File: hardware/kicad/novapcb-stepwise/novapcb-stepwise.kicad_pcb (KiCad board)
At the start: 6 copper layers, 105 x 85 mm, 129 parts, among them J1 USB-C_2.0, J10 CRSF_solder_pad, J11 ESC_solder_pad, J12 ESC_solder_pad, J13 ESC_solder_pad, J14 ESC_solder_pad, J15 ESC_solder_pad, J16 ESC_solder_pad, J17 ESC_solder_pad, J18 ESC_solder_pad, J19 MAUCH2_6P, J2 microSD_DM3AT, J20 CAN_4P, J3 TELEM_6P, J4 MAUCH_6P, J5 GPS_MAG_10P, J9 SWD_10P, Q2 AO3401A, Q3 AO4262E, Q4 AO4262E, Q5 AO3400A, U1 STM32H743VITx, U11 LM74700-Q1, U12 LM74700-Q1, U13 LP5907MFX-3.3, U14 TJA1051TK/3, U15 PESD2CAN, U2 AP2112K-3.3, U3 ICM-42688-P_LGA-14_2.5x3mm_P0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, U4 DPS310, U5 USBLC6-2P6, U6 TPS25940A, U7 LPS22HB, U8 BMI088, U9 LSM6DSV16X, Y1 8MHz

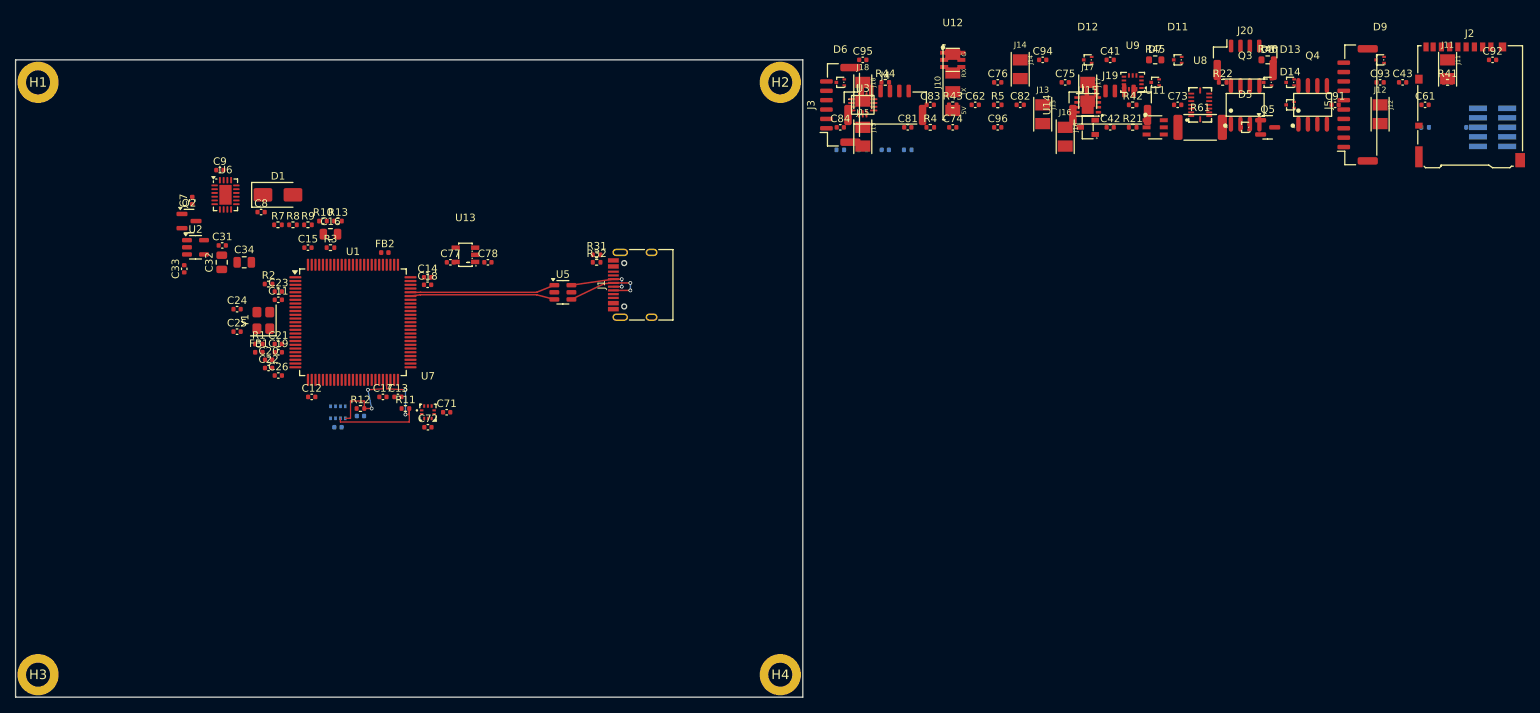
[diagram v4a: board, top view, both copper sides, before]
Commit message: hw: C↔B integration — +3V3 plane on In4.Cu + B-internal traces
Routes power rails B → C per master 2026-05-23 plan. DRC=0, gate12 v3
PASS at MCU 73.98°C (+6.02°C margin to 80°C, +1.02°C to lock target).

Strategy after F.Cu-zone + F.Cu-trace attempts surfaced MCU-pin-row +
GND-pad shorts: use inner-layer power plane.

  - +3V3 main rail: filled zone on In4.Cu, X=15..95, Y=18..52.
  - 18 vias at WIDE +3V3 pads (caps + sensor pads) connect F.Cu pad
    to In4.Cu plane.
  - 3 MCU VDD pins (U1.11, U1.75, U1.100) connected via 0.2mm F.Cu
    stubs to extra vias placed in clear space (avoiding Y1 GND, pin
    rows, and I2C2_SDA traces).
  - 2 MCU VDD pins (U1.27, U1.50) DEFERRED — south-stub crosses
    existing I2C2_SDA route; need B.Cu workaround in C↔E-2 step.
  - R11 +3V3 pull-up via DEFERRED — only marginal clearance (0.0035mm
    under rule) to existing I2C2_SDA via.

  - +3V3_IMU_PRE chain B-internal: FB2.2 → C77.1 → U13.1 + U13.3 stub.
    Routes use W=0.20mm and turn at (60.0, 24.0) to clear C77.2 GND
    and U13.4 NC pads (1.10mm wide SOT-23 pads — wider than expected).

  - +5V_BEC DEFERRED — discovered U2.1 input net is +5V (not +5V_BEC).
    The +5V source comes from A-zone Q3/Q4 OR-FETs which are unplaced.
    A↔B routing handles this in next phase.

Two placement fixes also in this commit:
  - update_outline_v11.py: hole inset 3.0 → 3.25mm so 5.5mm pads have
    0.5mm edge clearance (1.25mm fix preserves c-to-c ~98.5×78.5mm,
    within mechanical tolerance of master's "3mm inset" directive).
  - step5_place_B.py: C77 moved (58,27)→(56.5,27) so its GND pad
    clears U13.5 (+3V3_IMU) — pre-existing baseline DRC issue from
    the 105×85 outline transition.

gate12 v3 thermal check (full v1.1 load):
  Energy balance Q_in=1.7165 W, Q_out=1.7218 W, +0.31% PASS
  T_avg=69.29°C, T_max=78.14°C
  Tj_U1 (MCU) = 73.98°C  margin to 80°C = +6.02°C  LOCK
  Tj_U2 (LDO) = 70.01°C  margin to 80°C = +10.00°C LOCK
  All placed parts LOCK; planned positions (Q3, Q4, U14) TIGH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
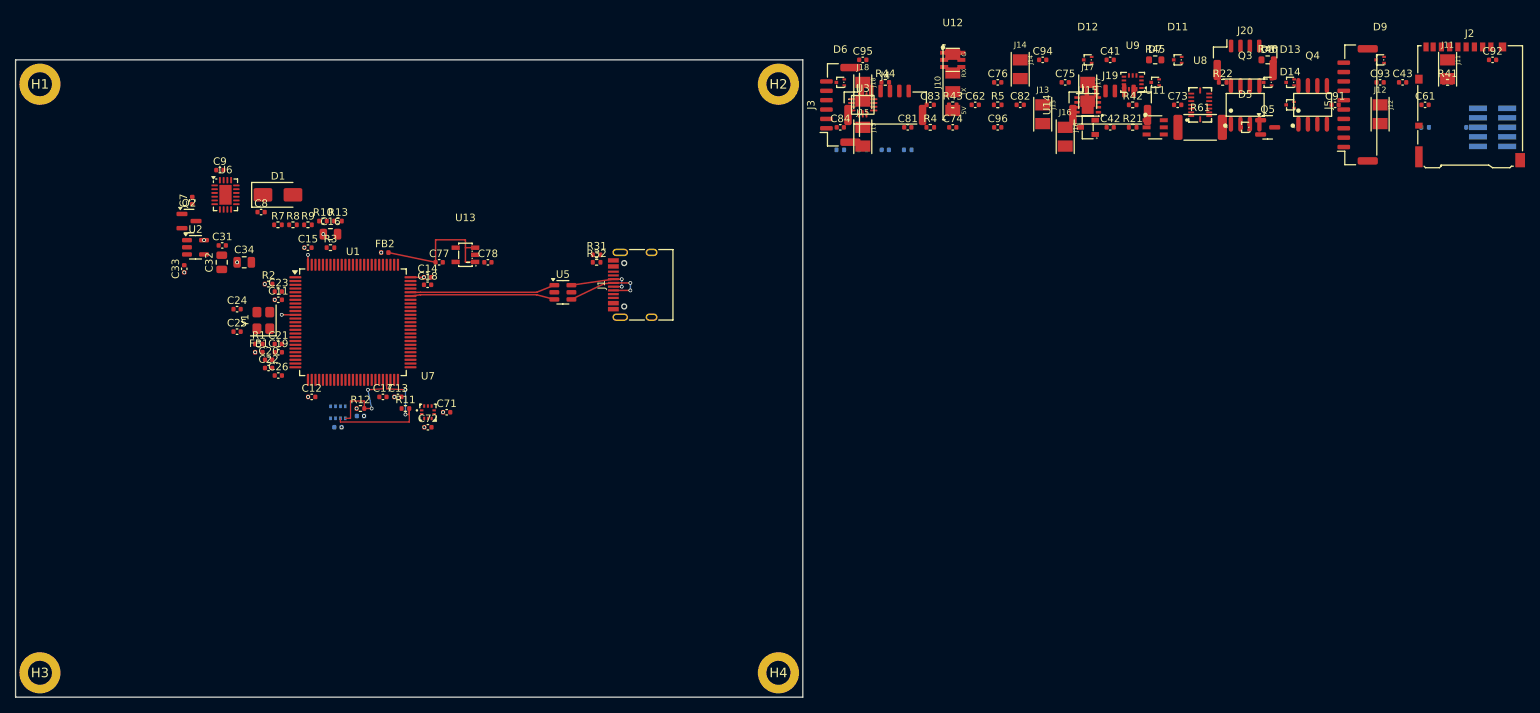
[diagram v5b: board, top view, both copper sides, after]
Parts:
- moved C77 1.50 mm to (56.5, 27.0)
- moved H1 0.35 mm to (3.25, 3.25)
- moved H2 0.35 mm to (101.8, 3.25)
- moved H3 0.35 mm to (3.25, 81.8)
- moved H4 0.35 mm to (101.8, 81.8)
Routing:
- net +3V3_IMU_PRE: track 0.00 -> 18.9 mm
- net +3V3: track 0.00 -> 4.96 mm, vias 0 -> 19
- added copper zone on In4.Cu, net +3V3
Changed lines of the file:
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@@
 	(footprint ""
 		(layer "F.Cu")
-		(at 102 82)
+		(at 101.75 81.75)
 		(property "Reference" "H4"
 			(at 0 0 0)
@@
 	(footprint ""
 		(layer "F.Cu")
-		(at 102 3)
+		(at 101.75 3.25)
 		(property "Reference" "H2"
 			(at 0 0 0)
@@
 	(footprint ""
 		(layer "F.Cu")
-		(at 3 3)
+		(at 3.25 3.25)
 		(property "Reference" "H1"
 			(at 0 0 0)
@@
 	(footprint "Capacitor_SMD:C_0402_1005Metric"
 		(layer "F.Cu")
-		(at 58 27)
+		(at 56.5 27)
 		(descr "Capacitor SMD 0402 (1005 Metric), square (rectangular) end terminal, IPC-7351 nominal, (Body size source: IPC-SM-782 page 76, https://www.pcb-3d.com/wordpress/wp-content/uploads/ipc-sm-782a_amendment_1_and_2.pdf), generated with kicad-footprint-generator")
 		(tags "capacitor")
@@
 	(footprint ""
 		(layer "F.Cu")
-		(at 3 82)
+		(at 3.25 81.75)
 		(property "Reference" "H3"
 			(at 0 0 0)
@@
 	)
 	(segment
+		(start 39 27.325)
+		(end 39 26)
+		(width 0.2)
+		(layer "F.Cu")
+		(net 1)
+	)
+	(segment
+		(start 37.325 34)
+		(end 35.5 34)
+		(width 0.2)
+		(layer "F.Cu")
+		(net 1)
+	)
+	(segment
+		(start 52.675 29)
+		(end 54.48 29)
+		(width 0.2)
+		(layer "F.Cu")
+		(net 1)
+	)
+	(via
+		(at 22.5 28.346025)
+		(size 0.5)
+		(drill 0.3)
+		(layers "F.Cu" "B.Cu")
+		(net 1)
+	)
+	(via
+		(at 41.05 23.245)
+		(size 0.5)
+		(drill 0.3)
+		(layers "F.Cu" "B.Cu")
+		(net 1)
+	)
+	(via
+		(at 35.5 34)
+		(size 0.5)
+		(drill 0.3)
+		(layers "F.Cu" "B.Cu")
+		(net 1)
+	)
+	(via
+		(at 33.235 29.9)
+		(size 0.5)
+		(drill 0.3)
+		(layers "F.Cu" "B.Cu")
+		(net 1)
+	)
+	(via
+		(at 50.52 44.955)
+		(size 0.5)
+		(drill 0.3)
+		(layers "F.Cu" "B.Cu")
+		(net 1)
+	)
+	(via
+		(at 48.765 25.700961)
+		(size 0.5)
+		(drill 0.3)
+		(layers "F.Cu" "B.Cu")
+		(net 1)
+	)
+	(via
+		(at 34.564999 32)
+		(size 0.5)
+		(drill 0.3)
+		(layers "F.Cu" "B.Cu")
+		(net 1)
+	)
+	(via
+		(at 46.48 47.5)
+		(size 0.5)
+		(drill 0.3)
+		(layers "F.Cu" "B.Cu")
+		(net 1)
+	)
+	(via
+		(at 43.48 49)
+		(size 0.5)
+		(drill 0.3)
+		(layers "F.Cu" "B.Cu")
+		(net 1)
+	)
+	(via
+		(at 39 26)
+		(size 0.5)
+		(drill 0.3)
+		(layers "F.Cu" "B.Cu")
+		(net 1)
+	)
+	(via
+		(at 45.49 46.5)
+		(size 0.5)
+		(drill 0.3)
+		(layers "F.Cu" "B.Cu")
+		(net 1)
+	)
+	(via
+		(at 25.1375 24.05)
+		(size 0.5)
+		(drill 0.3)
+		(layers "F.Cu" "B.Cu")
+		(net 1)
+	)
+	(via
+		(at 31.959999 39)
+		(size 0.5)
+		(drill 0.3)
+		(layers "F.Cu" "B.Cu")
+		(net 1)
+	)
+	(via
+		(at 39.02 44.955)
+		(size 0.5)
+		(drill 0.3)
+		(layers "F.Cu" "B.Cu")
+		(net 1)
+	)
+	(via
+		(at 54.475 29)
+		(size 0.5)
+		(drill 0.3)
+		(layers "F.Cu" "B.Cu")
+		(net 1)
+	)
+	(via
+		(at 29.55 27)
+		(size 0.5)
+		(drill 0.3)
+		(layers "F.Cu" "B.Cu")
+		(net 1)
+	)
+	(via
+		(at 38.52 25.045)
+		(size 0.5)
+		(drill 0.3)
+		(layers "F.Cu" "B.Cu")
+		(net 1)
+	)
+	(via
+		(at 54.52 49)
+		(size 0.5)
+		(drill 0.3)
+		(layers "F.Cu" "B.Cu")
+		(net 1)
+	)
+	(via
+		(at 57.02 47)
+		(size 0.5)
+		(drill 0.3)
+		(layers "F.Cu" "B.Cu")
+		(net 1)
+	)
+	(segment
+		(start 60 24)
+		(end 60 26.95)
+		(width 0.2)
+		(layer "F.Cu")
+		(net 4)
+	)
+	(segment
+		(start 60 26.95)
+		(end 61.3 26.95)
+		(width 0.2)
+		(layer "F.Cu")
+		(net 4)
+	)
+	(segment
+		(start 56.02 24)
+		(end 60 24)
+		(width 0.2)
+		(layer "F.Cu")
+		(net 4)
+	)
+	(segment
+		(start 56.02 27)
+		(end 56.02 24)
+		(width 0.2)
+		(layer "F.Cu")
+		(net 4)
+	)
+	(segment
+		(start 49.735 25.700961)
+		(end 56.02 27)
+		(width 0.2)
+		(layer "F.Cu")
+		(net 4)
+	)
+	(segment
+		(start 61.3 25.05)
+		(end 60 25.05)
+		(width 0.2)
+		(layer "F.Cu")
+		(net 4)
+	)
+	(segment
 		(start 49 43.875)
 		(end 47 44)
@@
 		(net 96)
 	)
+	(zone
+		(net 1)
+		(net_name "+3V3")
+		(layer "In4.Cu")
+		(hatch edge 0.5)
+		(connect_pads
+			(clearance 0.5)
+		)
+		(min_thickness 0.25)
+		(filled_areas_thickness no)
+		(fill
+			(thermal_gap 0.5)
+			(thermal_bridge_width 0.5)
+		)
+		(polygon
+			(pts
+				(xy 15 18) (xy 95 18) (xy 95 52) (xy 15 52)
+			)
+		)
+	)
 	(embedded_fonts no)

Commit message: hw: Step 6 — place A (POWER_INPUT) on 105×85 board, Q3/Q4 TIGHT→LOCK
Master 2026-05-23 sign-off after explicit constraint analysis.
22 components placed; DRC=0; gate12 v3 thermal predictions confirmed.

Layout:
- West cluster (X=12..40): J4 Mauch primary @ (15,5), D5/D6 TVS,
  U11 LM74700 ctrl @ (33,5), Q3 OR-FET @ (27,10)
- East cluster (X=68..95): J19 Mauch backup @ (90,5), D7/D8 TVS,
  U12 LM74700 ctrl @ (72,5), Q4 OR-FET @ (78,10)
- 51mm Q3↔Q4 separation (two physically-isolated BEC paths for EMI)
- Sense R+C in south band (Y=14.5) — north band conflicts with Q3/Q4
  pads (SO-8 pads extend Y=7.43..12.57, well outside courtyard
  Y=8..12). C9 in step5 moved (28,16)→(32,16) to clear A's R42 at
  X=28, Y=14.5.

gate12 v3 thermal (full v1.1 load, 105×85, MCU=0.700W):
  Energy balance Q_in=1.7165 W, Q_out=1.7218 W, +0.31% PASS
  T_avg=69.29°C, T_max=78.03°C

  Tj_U1 (MCU) = 73.89°C  +6.11°C  LOCK   (was +6.02 — held)
  Tj_Q3       = 71.32°C  +8.7°C   LOCK   (was 76.11 +3.9 TIGHT — gained +4.8°C)
  Tj_Q4       = 72.62°C  +7.4°C   LOCK   (was 75.69 +4.3 TIGHT — gained +3.1°C)
  Tj_U11      = 73.70°C  +6.3°C   LOCK
  Tj_U12      = 74.12°C  +5.9°C   LOCK
  Tj_U2       = 69.96°C  +10.0°C  LOCK
  Tj_U6       = 71.00°C  +9.0°C   LOCK
  Tj_U13      = 73.03°C  +7.0°C   LOCK
  Tj_Q2       = 69.01°C  +11.0°C  LOCK
  Tj_U14*     = 75.31°C  +4.7°C   TIGHT  (G zone planned, improves at G placement)

Master predictions held: Q3/Q4 promoted TIGHT→LOCK as planned;
MCU stayed at +6.1°C margin.

DRC=0 real, 186 unconnected (power rails not yet routed —
A↔B integration step handles P5V_BEC trunk).

Gate 2 renders committed: hardware/renders/step6_A/
  - top_full.png: full 105×85 board with A west+east clusters
  - zoom_A_west.png: J4/Q3/U11 cluster detail
  - zoom_A_east.png: J19/Q4/U12 cluster detail

Deferred to A↔B routing (next step):
- P5V_BEC trunk from Q3.5-8 and Q4.5-8 drains → U6 eFuse input.
  Inner-layer plane vs F.Cu trunk question: 6-layer stackup has
  In1/In2/In3.Cu empty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
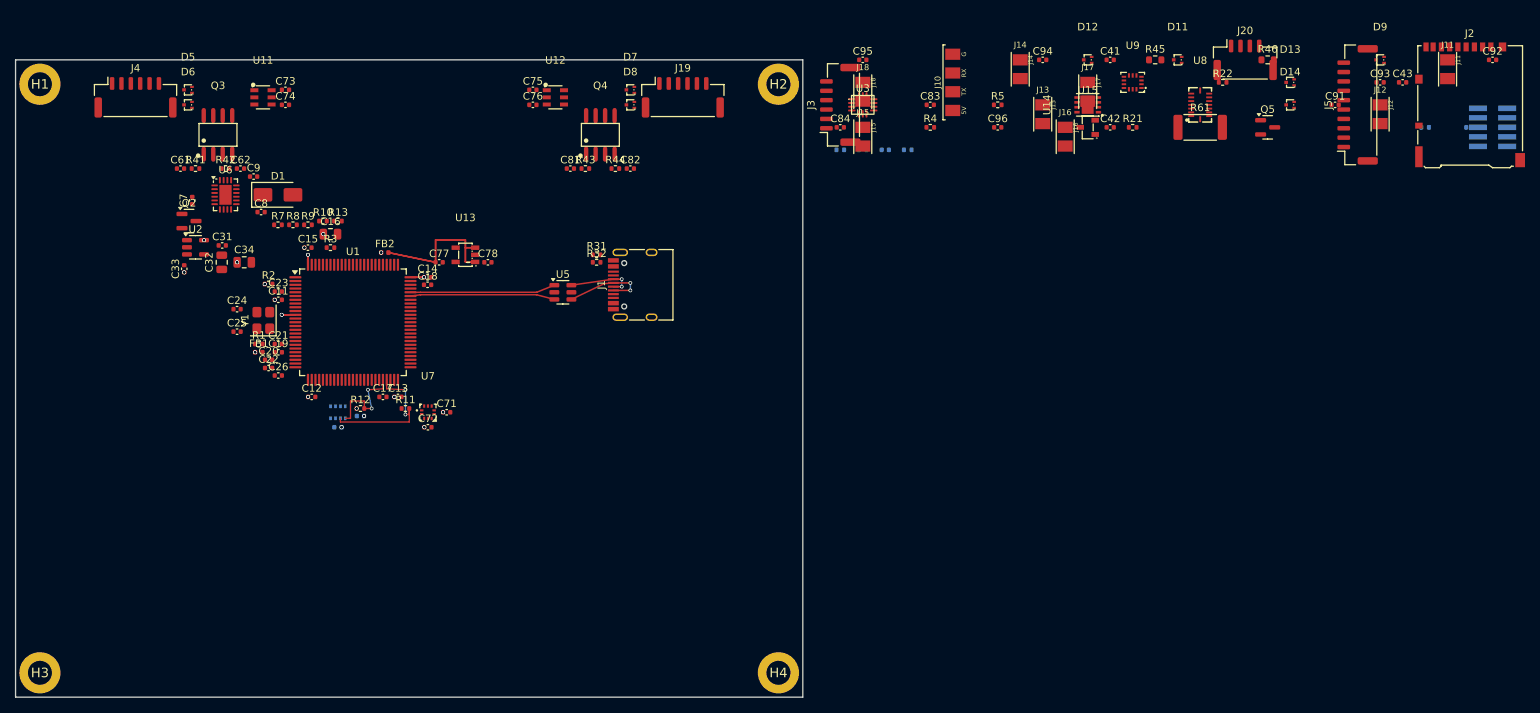
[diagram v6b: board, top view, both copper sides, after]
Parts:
- moved R41 167.4 mm to (24.0, 14.5)
- moved C61 166.2 mm to (22.0, 14.5)
- moved D5 141.1 mm to (23.0, 4.00)
- moved Q3 137.1 mm to (27.0, 10.0)
- moved R42 121.3 mm to (28.0, 14.5)
- moved U11 119.1 mm to (33.0, 5.00)
- moved C73 119.0 mm to (36.0, 4.00)
- moved J4 100.0 mm to (16.0, 5.00)
- moved C62 98.4 mm to (30.0, 14.5)
- moved Q4 95.1 mm to (78.0, 10.0)
- moved C74 89.1 mm to (36.0, 6.00)
- moved D6 87.1 mm to (23.0, 6.00)
- moved D8 85.1 mm to (82.0, 6.00)
- moved C75 71.0 mm to (69.0, 4.00)
- moved D7 70.0 mm to (82.0, 4.00)
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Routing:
- net +3V3_IMU_PRE: track 18.9 -> 37.9 mm
- net +3V3: track 4.96 -> 9.91 mm, vias 19 -> 38
